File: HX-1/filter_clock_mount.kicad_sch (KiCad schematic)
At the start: 27 parts, among them Y1 16MHz

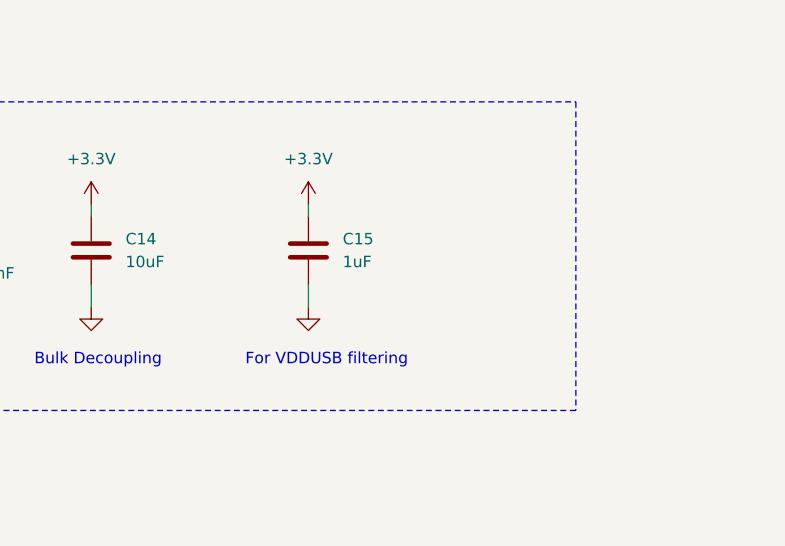
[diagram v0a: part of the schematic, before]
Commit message: add assembly files, fix reference designators
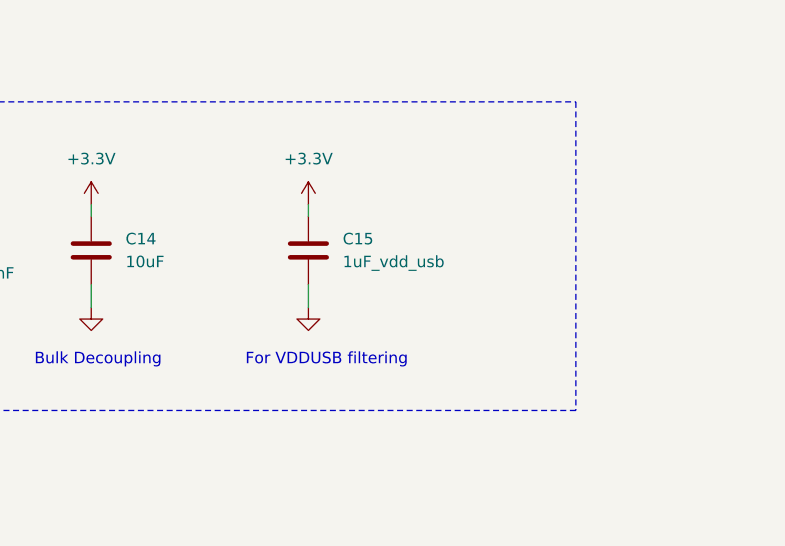
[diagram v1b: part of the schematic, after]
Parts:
- C15: value 1uF -> 1uF_vdd_usb
